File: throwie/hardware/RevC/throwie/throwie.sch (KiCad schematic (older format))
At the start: 24 parts, among them J1 CONN, Q1 2SC3356, Q2 SS8050-G, T1 TestPoints, T2 TestPoints, T3 TestPoints, T4 TestPoints, U1 C8051F850-A-GU, U2 MIC5231-3.3YM5-TR, X1 RO3101

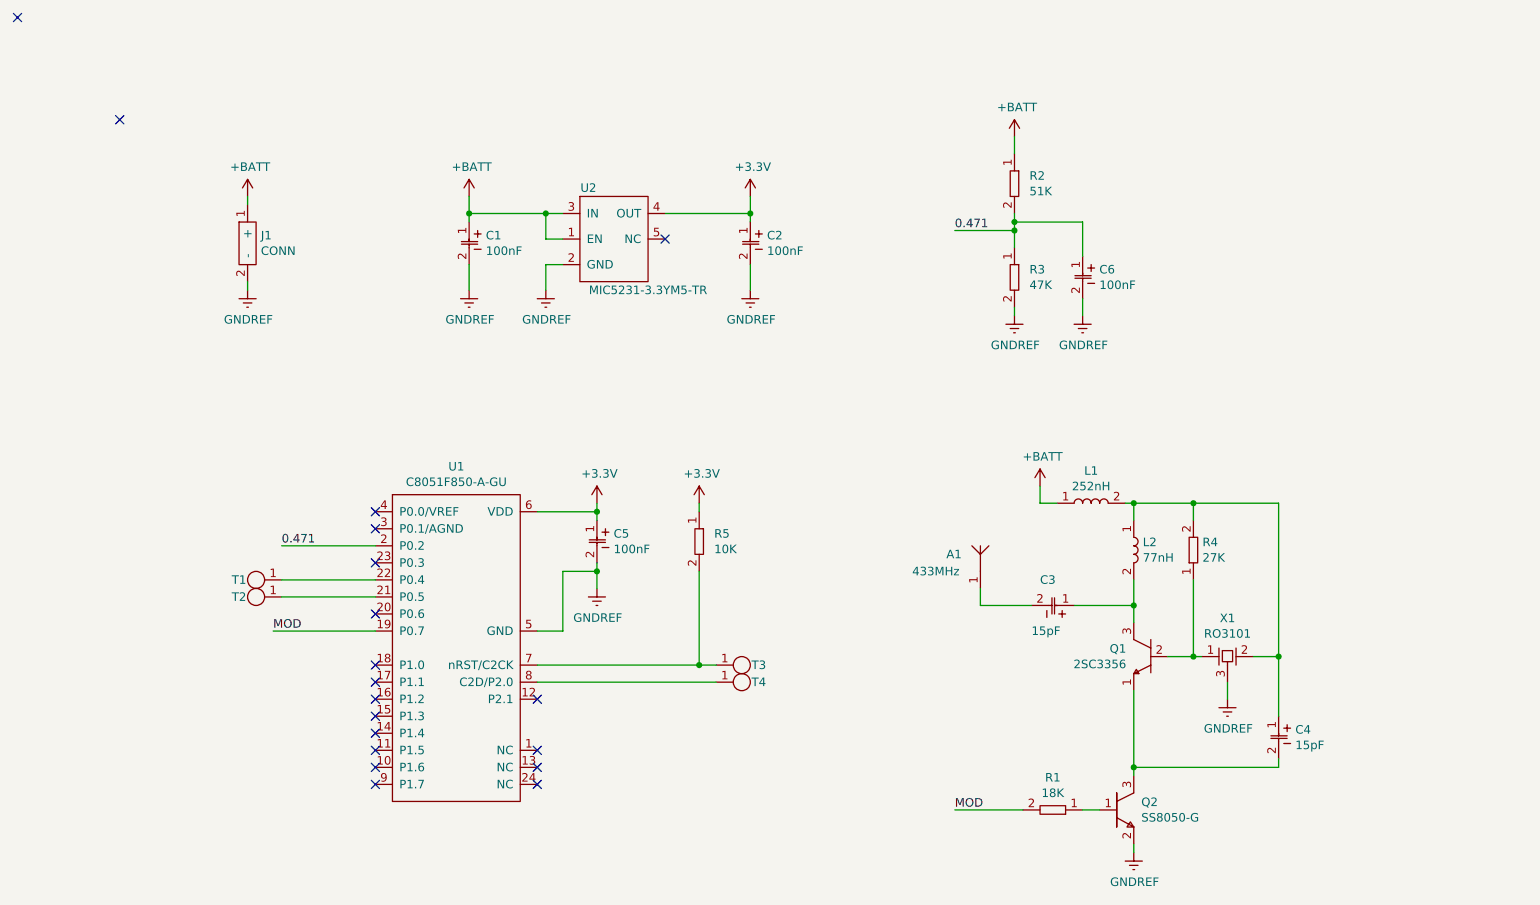
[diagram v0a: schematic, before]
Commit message: added more test points
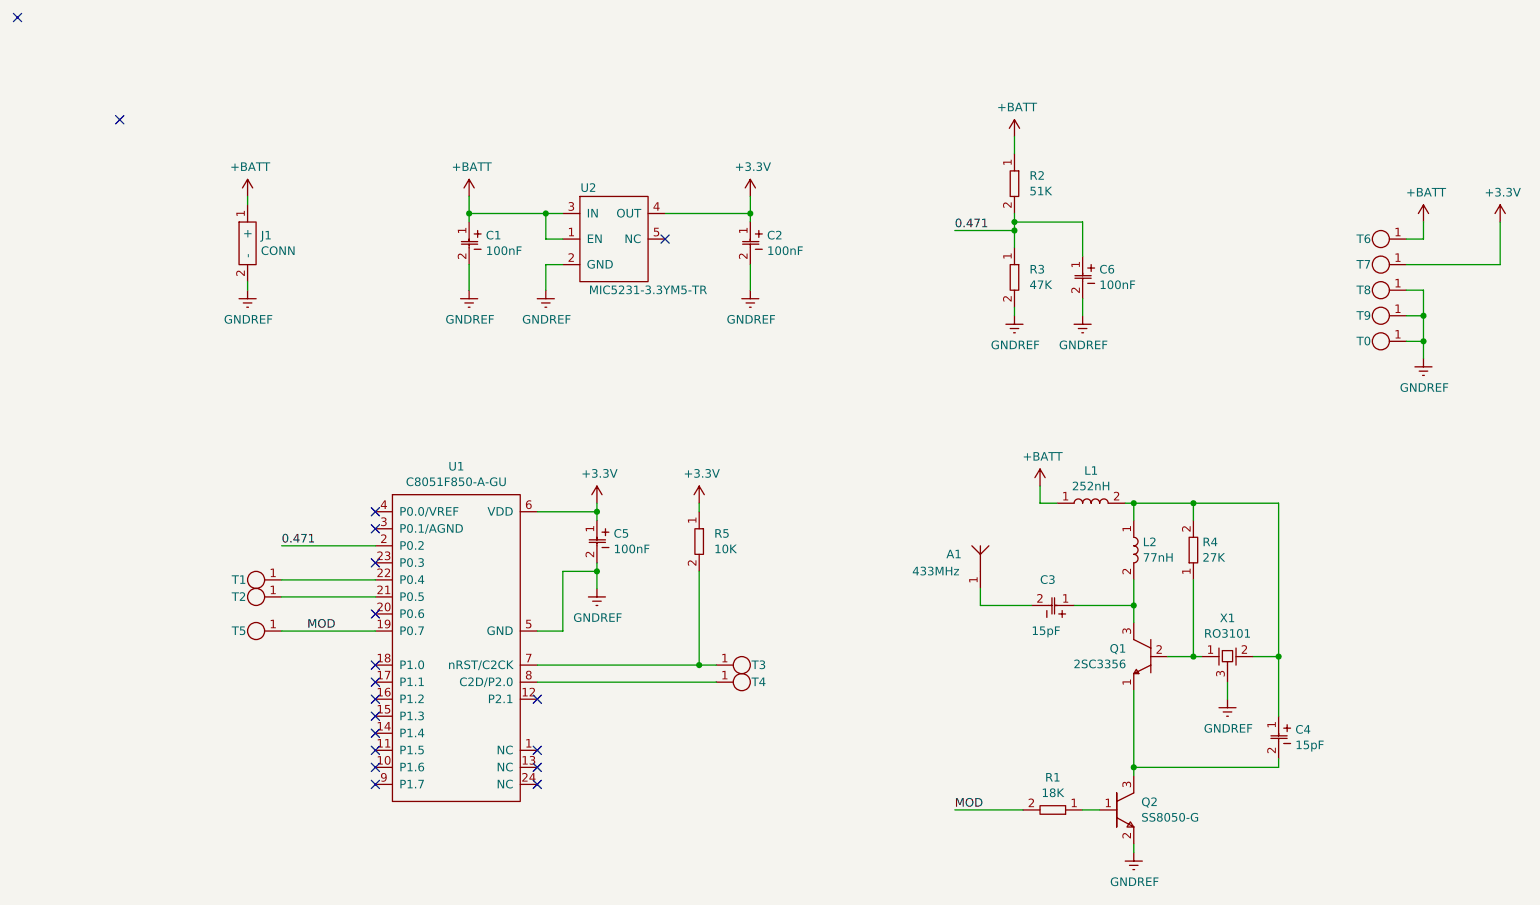
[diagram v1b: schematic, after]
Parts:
- added T0, T5, T6, T7, T8, T9: TestPoints, throwie:TestPoint, symbol throwie:TestPoints
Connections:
- net +3V3: now also T7.1
- net +BATT: now also T6.1
- net GNDREF: now also T0.1, T8.1, T9.1
- net MOD: now also T5.1
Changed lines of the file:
@@
 	6250 3050 6600 3050
 Connection ~ 6600 3050
-Text Label 1200 3800 0    50   ~ 0
+Text Label 1400 3800 0    50   ~ 0
 MOD
 Text Label 1250 3300 0    50   ~ 0
@@
 Wire Wire Line
 	1050 1800 1050 1750
-Wire Wire Line
-	1800 3800 1200 3800
 $Comp
 L throwie:CAP_0603 C6
@@
 NoConn ~ 1800 4400
 NoConn ~ 300  800
+$Comp
+L power:GNDREF #PWR0117
+U 1 1 62450E6E
+P 7950 2200
+F 0 "#PWR0117" H 7950 1950 50  0001 C CNN
+F 1 "GNDREF" H 7955 2027 50  0000 C CNN
+F 2 "" H 7950 2200 50  0001 C CNN
+F 3 "" H 7950 2200 50  0001 C CNN
+	1    7950 2200
+	1    0    0    -1
+$EndComp
+$Comp
+L power:+3.3V #PWR0118
+U 1 1 62453602
+P 8400 1400
+F 0 "#PWR0118" H 8400 1250 50  0001 C CNN
+F 1 "+3.3V" H 8415 1573 50  0000 C CNN
+F 2 "" H 8400 1400 50  0001 C CNN
+F 3 "" H 8400 1400 50  0001 C CNN
+	1    8400 1400
+	1    0    0    -1
+$EndComp
+$Comp
+L power:+BATT #PWR0119
+U 1 1 62453A01
+P 7950 1400
+F 0 "#PWR0119" H 7950 1250 50  0001 C CNN
+F 1 "+BATT" H 7965 1573 50  0000 C CNN
+F 2 "" H 7950 1400 50  0001 C CNN
+F 3 "" H 7950 1400 50  0001 C CNN
+	1    7950 1400
+	1    0    0    -1
+$EndComp
+$Comp
+L throwie:TestPoints T5
+U 1 1 62455406
+P 1250 3800
+F 0 "T5" H 1500 3800 50  0000 C CNN
+F 1 "TestPoints" H 1150 3550 50  0001 C CNN
+F 2 "throwie:TestPoint" H 1250 3800 50  0001 C CNN
+F 3 "" H 1250 3800 50  0001 C CNN
+	1    1250 3800
+	-1   0    0    1
+$EndComp
+Wire Wire Line
+	1800 3800 1250 3800
+$Comp
+L throwie:TestPoints T9
+U 1 1 6245B4E4
+P 7850 1950
+F 0 "T9" H 8100 1950 50  0000 C CNN
+F 1 "TestPoints" H 7750 1700 50  0001 C CNN
+F 2 "throwie:TestPoint" H 7850 1950 50  0001 C CNN
+F 3 "" H 7850 1950 50  0001 C CNN
+	1    7850 1950
+	-1   0    0    1
+$EndComp
+$Comp
+L throwie:TestPoints T8
+U 1 1 6245CE73
+P 7850 1800
+F 0 "T8" H 8100 1800 50  0000 C CNN
+F 1 "TestPoints" H 7750 1550 50  0001 C CNN
+F 2 "throwie:TestPoint" H 7850 1800 50  0001 C CNN
+F 3 "" H 7850 1800 50  0001 C CNN
+	1    7850 1800
+	-1   0    0    1
+$EndComp
+$Comp
+L throwie:TestPoints T7
+U 1 1 6245D151
+P 7850 1650
+F 0 "T7" H 8100 1650 50  0000 C CNN
+F 1 "TestPoints" H 7750 1400 50  0001 C CNN
+F 2 "throwie:TestPoint" H 7850 1650 50  0001 C CNN
+F 3 "" H 7850 1650 50  0001 C CNN
+	1    7850 1650
+	-1   0    0    1
+$EndComp
+$Comp
+L throwie:TestPoints T6
+U 1 1 6245D2AC
+P 7850 1500
+F 0 "T6" H 8100 1500 50  0000 C CNN
+F 1 "TestPoints" H 7750 1250 50  0001 C CNN
+F 2 "throwie:TestPoint" H 7850 1500 50  0001 C CNN
+F 3 "" H 7850 1500 50  0001 C CNN
+	1    7850 1500
+	-1   0    0    1
+$EndComp
+Wire Wire Line
+	7950 1400 7950 1500
+Wire Wire Line
+	7950 1500 7850 1500
+Wire Wire Line
+	7850 1650 8400 1650
+Wire Wire Line
+	8400 1650 8400 1400
+Wire Wire Line
+	7850 1800 7950 1800
+Wire Wire Line
+	7950 1800 7950 1950
+Wire Wire Line
+	7850 1950 7950 1950
+Connection ~ 7950 1950
+$Comp
+L throwie:TestPoints T0
+U 1 1 624758B1
+P 7850 2100
+F 0 "T0" H 8100 2100 50  0000 C CNN
+F 1 "TestPoints" H 7750 1850 50  0001 C CNN
+F 2 "throwie:TestPoint" H 7850 2100 50  0001 C CNN
+F 3 "" H 7850 2100 50  0001 C CNN
+	1    7850 2100
+	-1   0    0    1
+$EndComp
+Wire Wire Line
+	7950 1950 7950 2100
+Wire Wire Line
+	7850 2100 7950 2100
+Connection ~ 7950 2100
+Wire Wire Line
+	7950 2100 7950 2200
 $EndSCHEMATC
